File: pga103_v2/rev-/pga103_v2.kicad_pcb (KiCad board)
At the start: 2 copper layers, 38.1 x 25.4 mm, 30 parts, among them J1 RF_IN, J2 RF_OUT, U1 SPX3819M5-L-5-0, U2 PGA-103, U3 RBP-XXX

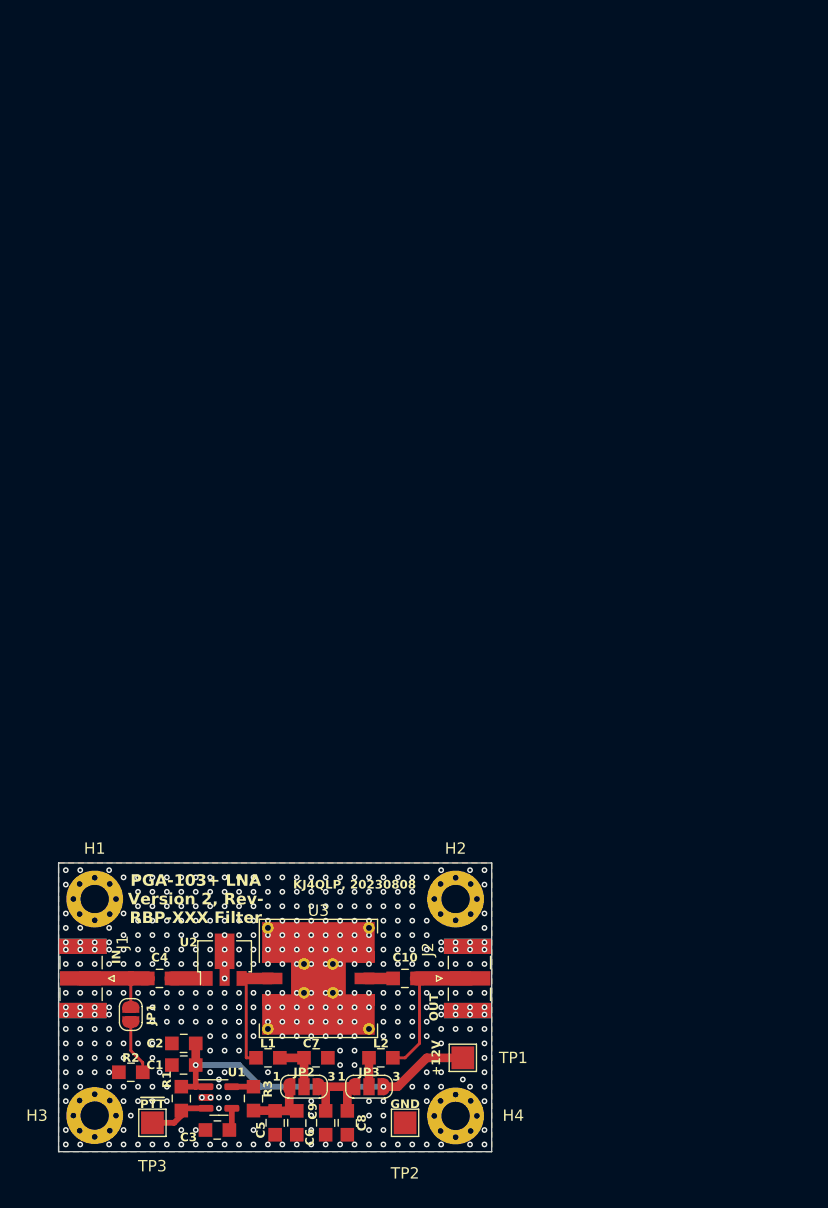
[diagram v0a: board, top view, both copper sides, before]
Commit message: aded gitignore, about to rearrange for MAJOR.MINOR.PATCH versioning
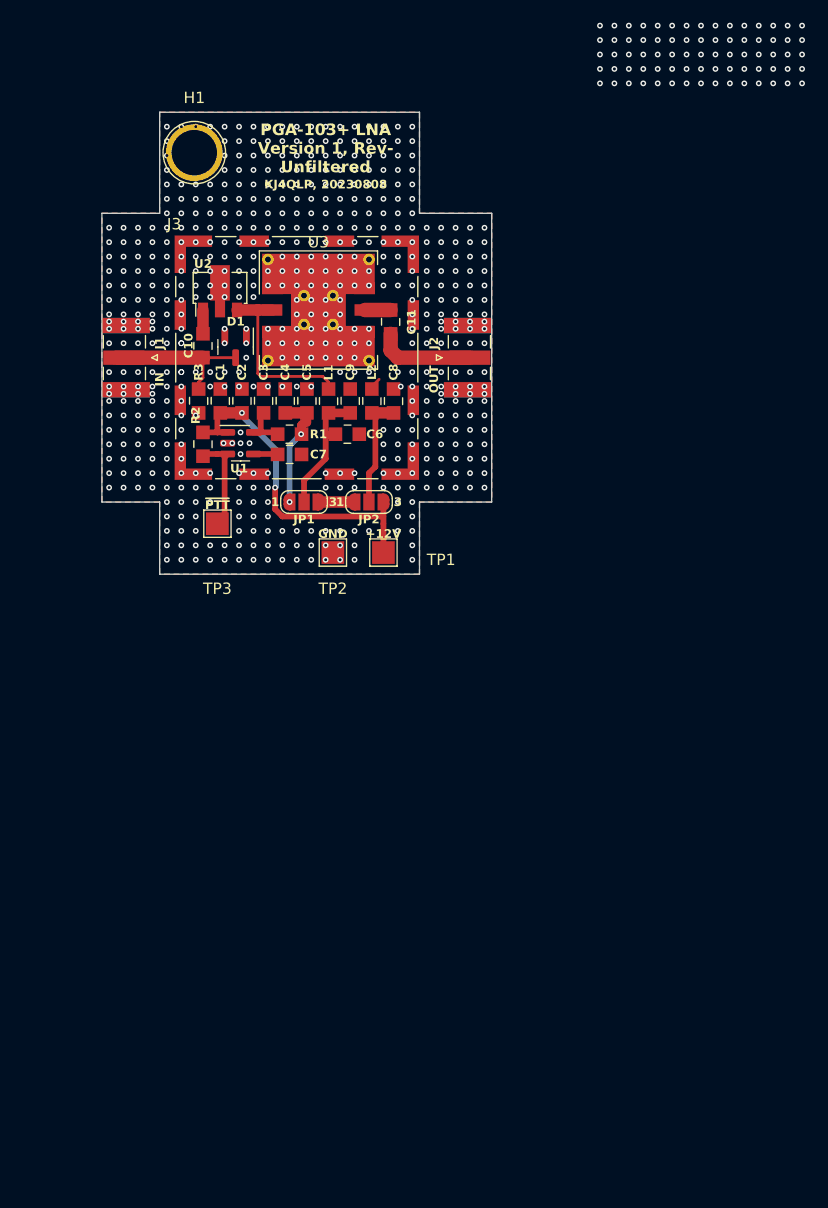
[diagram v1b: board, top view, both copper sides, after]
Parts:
- removed H2, H3, H4: Hole, MountingHole:MountingHole_2.5mm_Pad_Via
- removed the JP1 at (101.6, 114.9)
- added C3: 0.1uF, digikey-footprints:0805, F.Cu at (113.3, 61.0)
- added D1: BAV99, Package_TO_SOT_SMD:SOT-23, F.Cu at (110.8, 56.2)
- added J3: RFShield_TwoPieces, RF_Shielding:Wuerth_36103205_20x20mm, F.Cu at (116.2, 57.1)
- C1: value 1uF -> 1.0uF
- C10: renamed from C4; value 18pF -> 1000pF
- C11: renamed from C10; value 18pF -> 1000pF
- C5: renamed from C6; value 0.1uF -> 1.0uF
- C8: value 1uF -> 1000pF
- C9: renamed from C7; value 18pF -> 1000pF
- H1: footprint MountingHole:MountingHole_2.5mm_Pad_Via -> TestPoint:TestPoint_Plated_Hole_D4.0mm
- L1: value 56nH -> 220nH
- L2: value 470uH -> 220nH
- R1: renamed from R3; value 0 -> 10
- U3: value RBP-XXX -> RBP-140/440
- moved H1 66.2 mm to (107.2, 39.1)
- moved C8 63.6 mm to (124.7, 61.0)
- moved C4 63.5 mm to (115.2, 61.0), turned to -90 degrees
- moved C5 63.5 mm to (117.1, 61.0), turned to -90 degrees
- moved C6 60.6 mm to (120.7, 63.9), turned to 180 degrees
- moved C7 59.8 mm to (115.6, 65.7), turned to 180 degrees
- moved R3 59.4 mm to (107.6, 61.0), turned to -90 degrees
- moved U2 58.8 mm to (109.5, 51.0)
- moved U3 58.8 mm to (118.1, 53.0)
- moved R1 58.5 mm to (115.6, 63.9), turned to 0 degrees
- moved C1 58.5 mm to (109.5, 61.0), turned to -90 degrees
- moved L1 58.0 mm to (119.0, 61.0), turned to 90 degrees
- moved C9 57.9 mm to (120.9, 61.0), turned to -90 degrees
- moved L2 57.8 mm to (122.8, 61.0), turned to 90 degrees
- moved C11 57.8 mm to (124.5, 54.0), turned to -90 degrees
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- renumbered C5 to C4, C9 to C6, C3 to C7, JP2 to JP1, JP3 to JP2, R1 to R2, R2 to R3
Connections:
- C6 pad 2: Net-(JP2-B) -> Net-(JP1-C)
- C8 pad 1: GND -> Net-(JP2-C)
- C8 pad 2: Net-(JP2-B) -> GND
- C9 pad 2: Net-(JP2-C) -> Net-(JP1-C)
- JP1 pad 2: Net-(JP2-C) -> Net-(JP1-C)
- JP1 pad 3: Net-(JP2-B) -> Net-(JP1-B)
- JP2 pad 1: Net-(JP2-B) -> Net-(JP1-B)
- JP2 pad 2: Net-(JP3-C) -> Net-(JP2-C)
- L1 pad 1: Net-(JP2-C) -> Net-(JP1-C)
- L2 pad 1: Net-(JP3-C) -> Net-(JP2-C)
- R3 pad 1: Net-(JP1-B) -> Net-(J1-In)
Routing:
- net Net-(JP1-C): track 0.00 -> 11.5 mm
- net Net-(JP2-B): track 8.57 -> 0.00 mm
- net Net-(U3-IN): track 10.5 -> 15.8 mm
- net Net-(J1-In): track 8.44 -> 13.4 mm
- net Net-(JP2-C): track 4.66 -> 9.42 mm
- net +5V: track 5.96 -> 10.3 mm, vias 0 -> 2
- net Net-(J2-In): track 14.0 -> 9.82 mm
- net Net-(U1-EN): track 5.50 -> 8.75 mm
- net Net-(JP3-C): track 2.54 -> 0.00 mm
- net Net-(U1-OUT): track 1.91 -> 3.90 mm
- net Net-(JP1-B): track 4.86 -> 3.11 mm
- net +12V: track 31.3 -> 29.9 mm
- net Net-(C10-Pad2): track 3.17 -> 2.09 mm
- net GND: vias 403 -> 651
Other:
- board size 38.1 x 25.4 mm -> 34.3 x 40.6 mm
- board text added: "JP1"
- board text added: "PGA-103+ LNA Version 1, Rev- Unfiltered"
- board text removed: "#2"
- board text removed: "0.75{dblquote}"
- board text removed: "1.0{dblquote}"
- board text removed: "1.5{dblquote}"
- board text removed: "BND:"
- board text removed: "JP3"
- board text removed: "Jumper Setting"
- board text removed: "PGA-103+ LNA Version 2, Rev- RBP-XXX Filter"
- board text removed: "RBP-"
